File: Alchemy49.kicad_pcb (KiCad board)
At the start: 2 copper layers, 267.5 x 76.2 mm, 205 parts, among them J1 USB_B_Micro, J2 Conn_01x05_Female, Q1 2N7002E, SW1 ESC-1.5U, SW10 O-1U, SW11 P-1U, SW12 BACK-1.5U, SW13 DEL-1U, SW14 TAB-1.75U, SW15 A-1U, SW16 S-1U, SW17 D-1U, SW18 F-1U, SW19 G-1U, SW2 Q-1U, SW20 H-1U, SW21 J-1U, SW22 K-1U, SW23 L-1U, SW24 ENTER-2.25U, SW25 PGUP-1U, SW26 SHIFT-2U, SW27 Z-1U, SW28 X-1U, SW29 C-1U, SW3 W-1U, SW30 V-1U, SW31 B-1U, SW32 N-1U, SW33 M-1U, SW34 COM-1U, SW35 PER-1U, SW36 SLASH-1U, SW37 UP-1U, SW38 PGDN-1U, SW39 CTRL1-1U, SW4 E-1U, SW40 WIN-1U, SW41 ALT-1U, SW42 FN1-1U, SW43 SPACE-2.75U, SW44 SHIFT-2.25U, SW45 FN2-1U, SW46 CTRL2-1U, SW47 LEFT-1U, SW48 DOWN-1U, SW49 RIGHT-1U, SW5 R-1U, SW6 T-1U, SW7 Y-1U, SW8 U-1U, SW9 I-1U

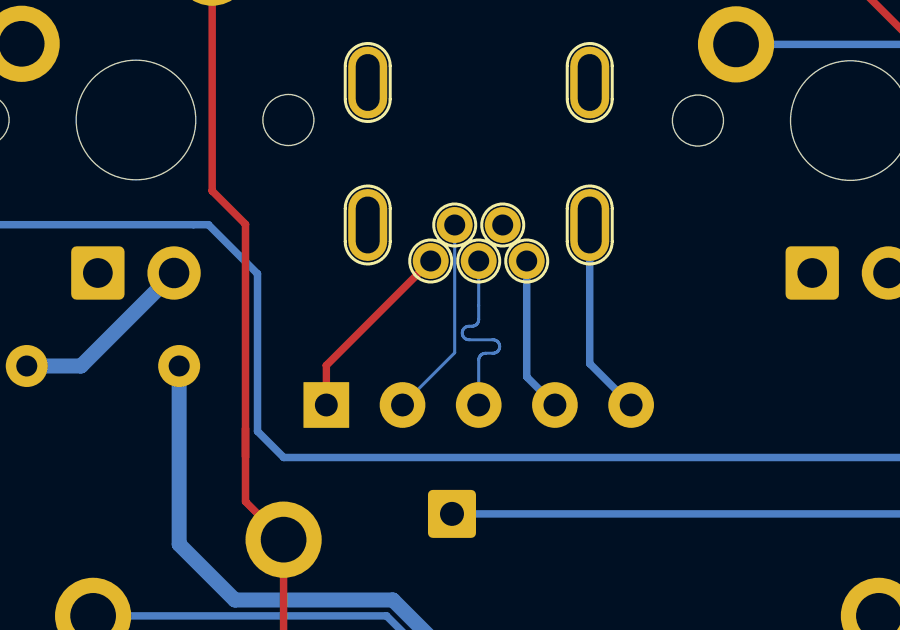
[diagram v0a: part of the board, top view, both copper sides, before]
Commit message: Rerouted the USB data lines
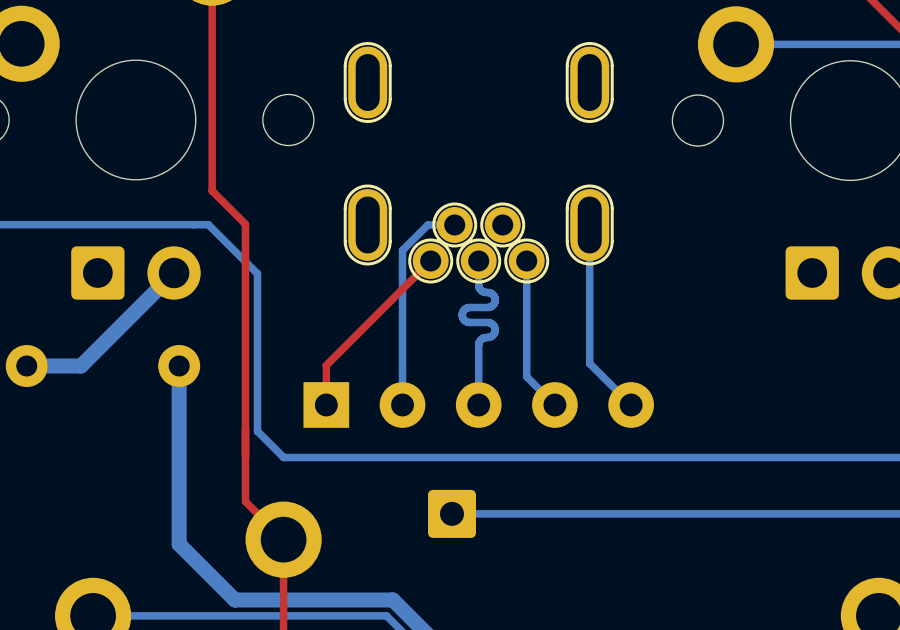
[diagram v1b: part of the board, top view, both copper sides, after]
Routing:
- net Net-(J1-Pad2): track 6.72 -> 7.25 mm
- net Net-(J1-Pad3): track 6.72 -> 7.24 mm
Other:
- net class USB: trace_width 0.1 -> 0.25

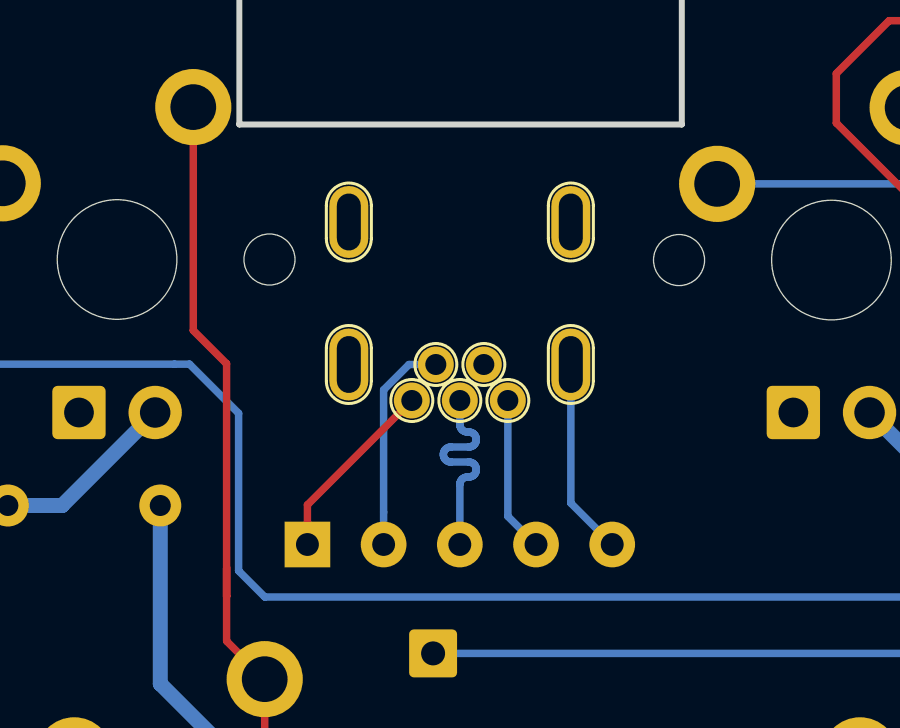
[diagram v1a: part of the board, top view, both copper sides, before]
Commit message: Updated to new XM7D footprint in the Acheron Library
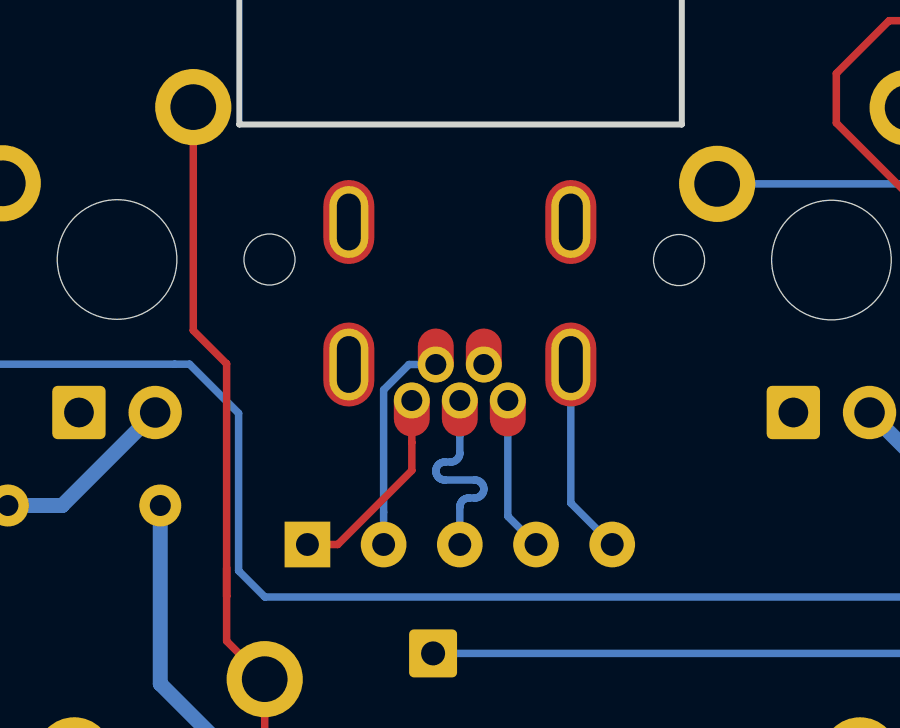
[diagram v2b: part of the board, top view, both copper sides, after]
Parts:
- B1: value SPARKFUN_PRO_MICRO -> >VALUE; footprint SPARKFUN_PRO_MICRO -> SparkFun_Boards:SPARKFUN_PRO_MICRO
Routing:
- net Net-(J1-Pad1): track 6.24 -> 6.83 mm
